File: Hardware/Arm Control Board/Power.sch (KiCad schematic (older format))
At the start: 73 parts

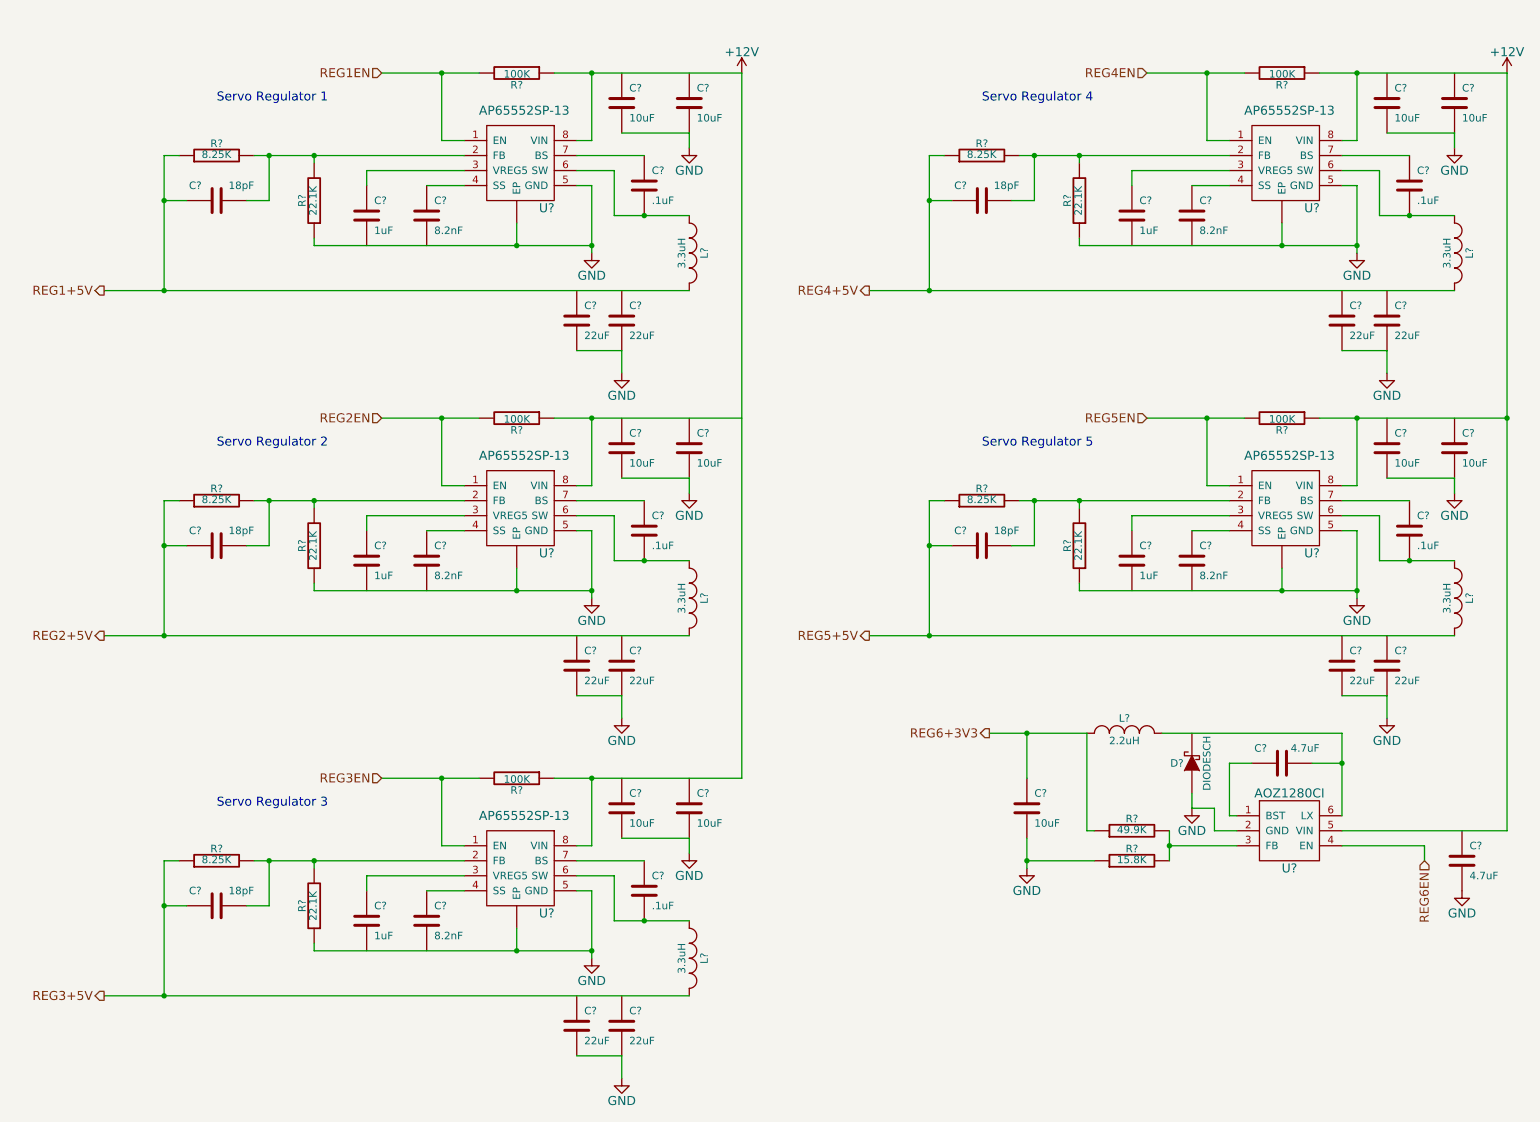
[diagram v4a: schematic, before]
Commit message: Fixed some floating wires
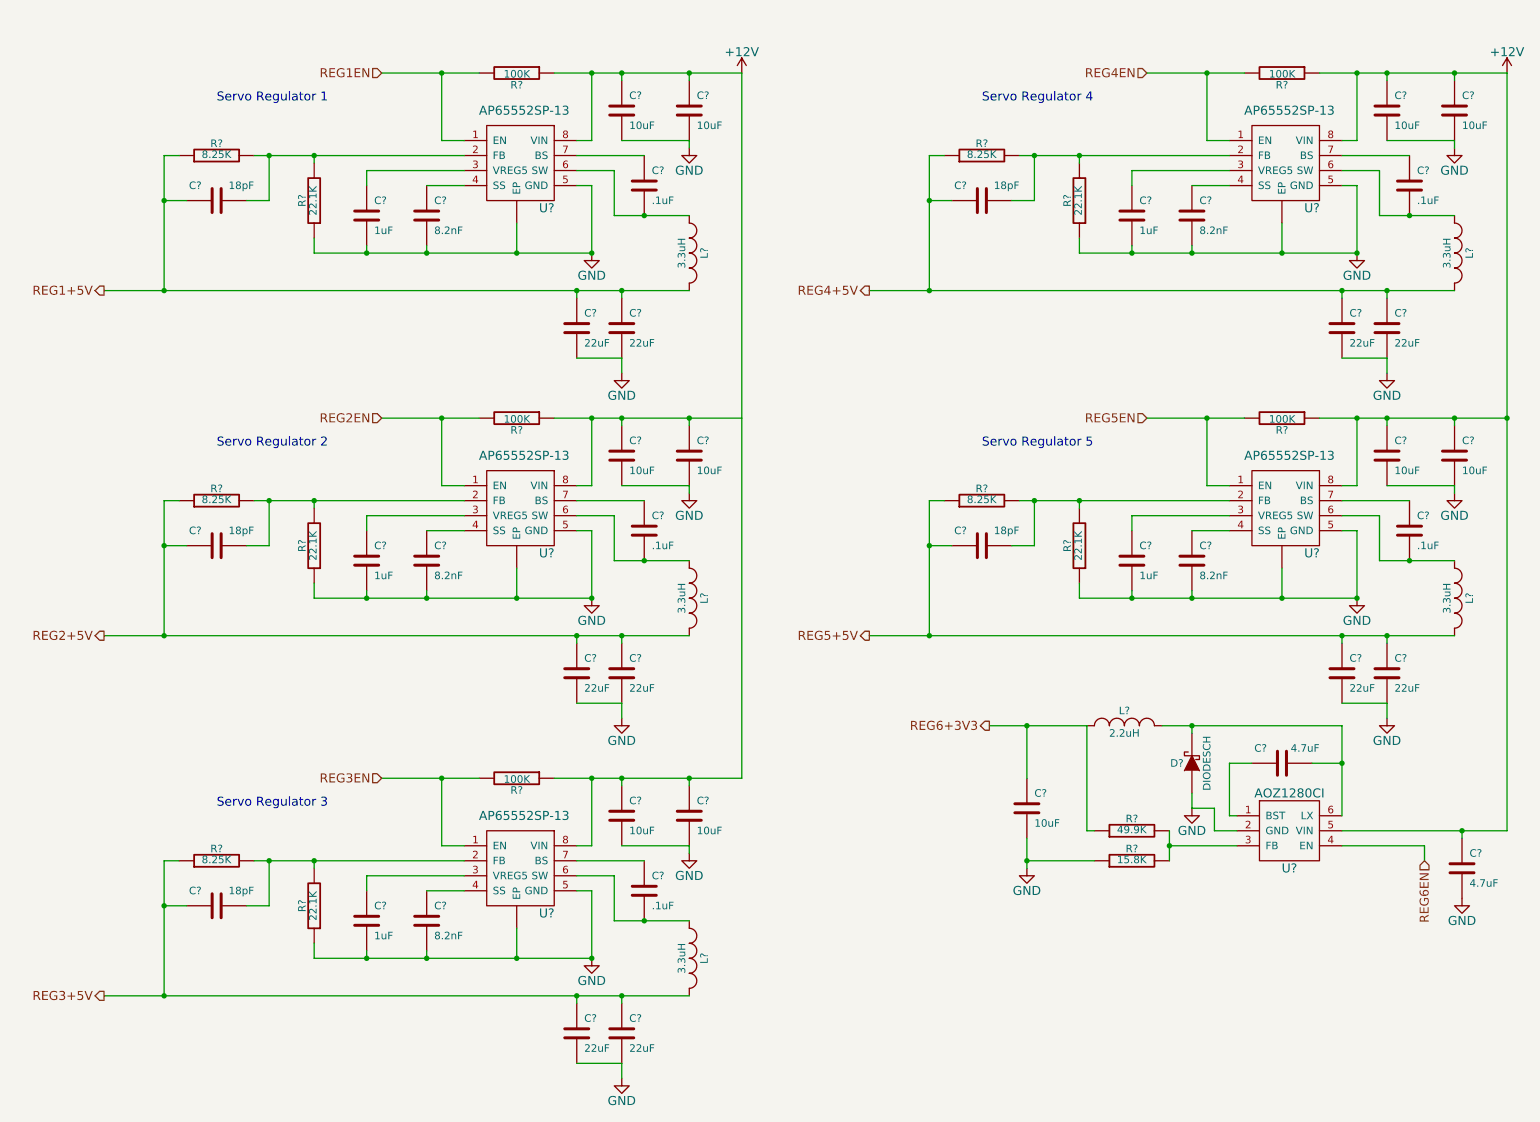
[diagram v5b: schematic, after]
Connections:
- net +12V: now also C?.1, C?.1, C?.1, C?.1, C?.1, C?.1, C?.1, C?.1, C?.1
- net GND: now also C?.2, C?.2, C?.2, C?.2, C?.2, C?.2, C?.2, C?.2, C?.2, C?.2
- net REG1+5V: now also C?.1, C?.1
- net REG2+5V: now also C?.1, C?.1
- net REG3+5V: now also C?.1, C?.1
- net REG4+5V: now also C?.1, C?.1
- net REG5+5V: now also C?.1, C?.1
- net at R?.1, U?.8 (VIN): now also C?.1, C?.1
- net at C?.2, L?.2, U?.6 (LX): now also D?.2 (K)
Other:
- moved on the sheet: C?, L?

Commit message: Reorganized regulators, added 5V reg, ext osc, PNs
Way too much for one commit, sorry about that. Reorganized the
regulators into high voltage/low voltage sheets. Added product numbers
to all passives + more. Check issues for any other changes
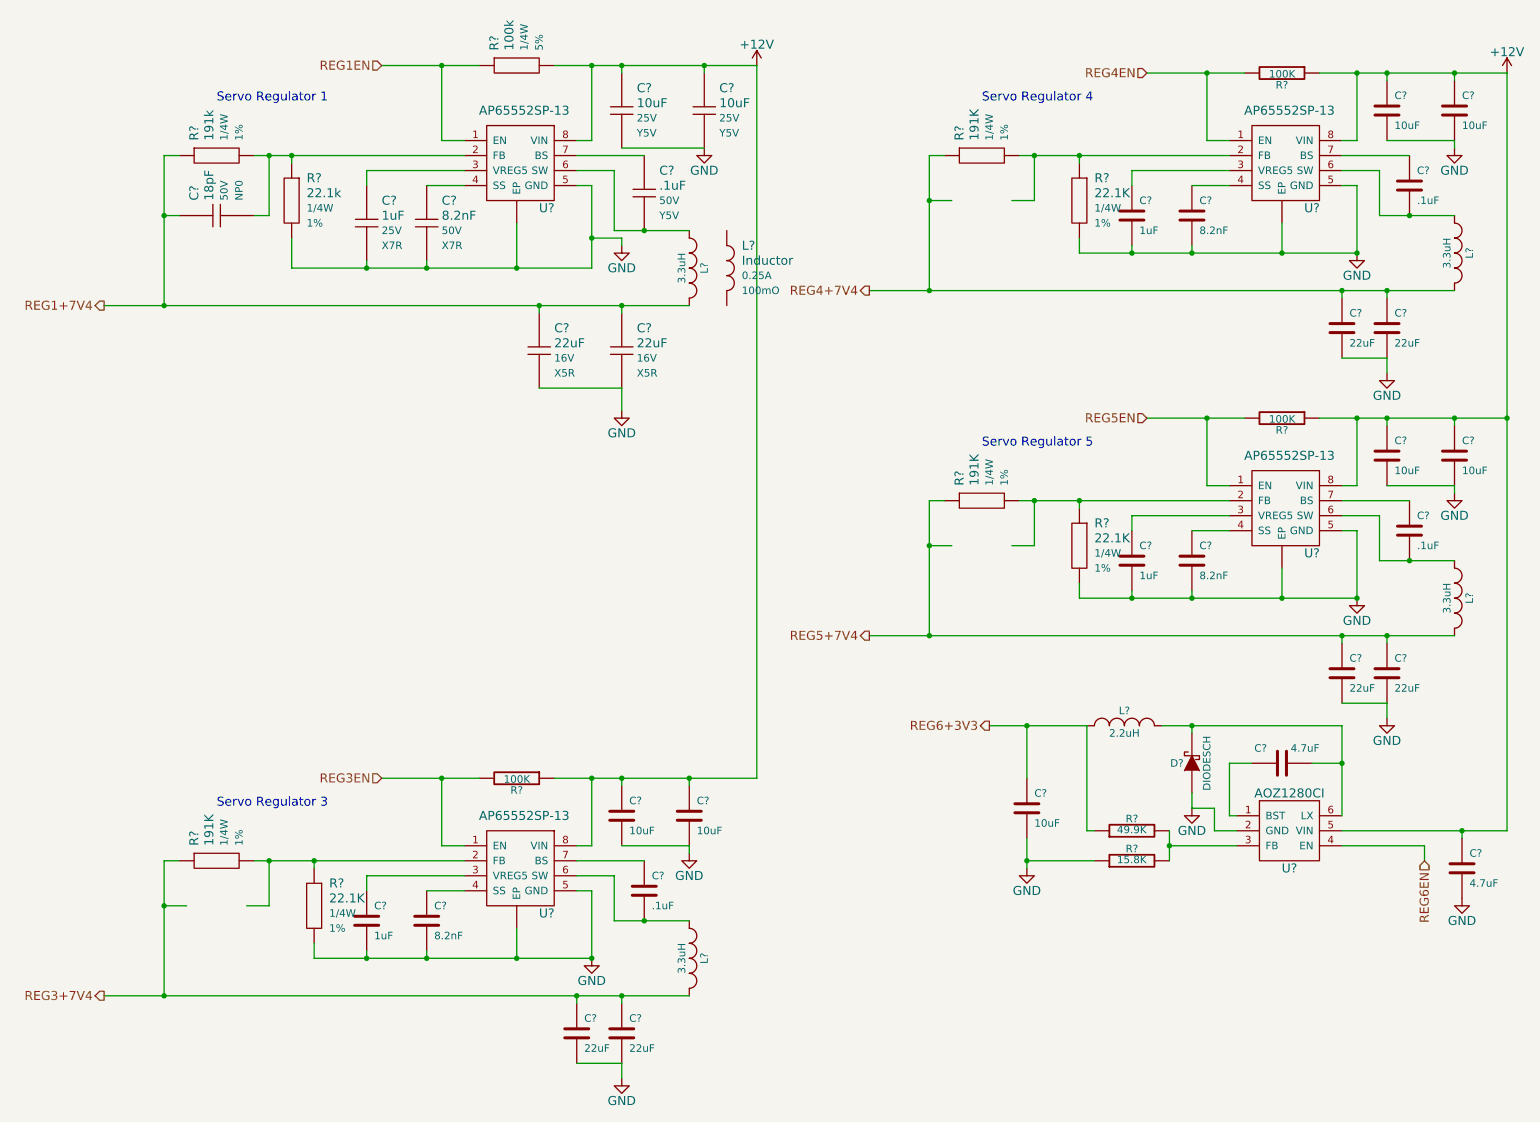
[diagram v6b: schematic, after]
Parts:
- removed C? (x4): 10uF, symbol C
- removed C? (x2): .1uF, symbol C
- removed C? (x4): 22uF, symbol C
- removed C? (x2): 8.2nF, symbol C
- removed C? (x2): 1uF, symbol C
- removed C? (x5): 18pF, symbol C
- removed L?: 3.3uH, symbol INDUCTOR_SMALL
- removed R? (x2): 100K, symbol R
- removed R? (x5): 22.1K, symbol R
- removed R? (x5): 8.25K, symbol R
- removed U?: AP65552SP-13, symbol AP65552SP-13
- added C?: 18pF, Capacitors_SMD:C_1206_HandSoldering, symbol Capacitor
- added C?: 1uF, Capacitors_SMD:C_1206_HandSoldering, symbol Capacitor
- added C?: 8.2nF, Capacitors_SMD:C_1206_HandSoldering, symbol Capacitor
- added C?: .1uF, Capacitors_SMD:C_1206_HandSoldering, symbol Capacitor
- added C? (x2): 22uF, Capacitors_SMD:C_1206_HandSoldering, symbol Capacitor
- added C? (x2): 10uF, Capacitors_SMD:C_1206_HandSoldering, symbol Capacitor
- added L?: Inductor, symbol Inductor
- added R?: 191k, Resistors_SMD:R_1206_HandSoldering, symbol Resistor
- added R? (x3): 191K, Resistors_SMD:R_1206_HandSoldering, symbol Resistor
- added R?: 22.1k, Resistors_SMD:R_1206_HandSoldering, symbol Resistor
- added R? (x3): 22.1K, Resistors_SMD:R_1206_HandSoldering, symbol Resistor
- added R?: 100k, Resistors_SMD:R_1206_HandSoldering, symbol Resistor
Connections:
- net labels added: REG1+7V4, REG3+7V4, REG4+7V4, REG5+7V4
- net labels removed: REG1+5V, REG2+5V, REG2EN, REG3+5V, REG4+5V, REG5+5V
- wire segments 282 -> 235
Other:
- note removed: "Servo Regulator 2"
- moved on the sheet: L?
